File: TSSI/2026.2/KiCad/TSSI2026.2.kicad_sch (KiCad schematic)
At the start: 32 parts, among them J1 Conn_01x02, J2 Conn_01x02, J3 Conn_02x02, Q1 IRLZ34N, T555 Test555, U1 LM555xN, U2 IRLZ34N, U3 4069, U3 IRLZ34N, U4 4001

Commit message: Add files via upload
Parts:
- removed U3: 4069, Package_SO:SOIC-14_3.9x8.7mm_P1.27mm, symbol 4xxx:4069
- removed unit 7 of U3
- added U5: 4069, Package_SO:SOIC-14_3.9x8.7mm_P1.27mm, symbol 4xxx:4069
- U3: footprint Package_SO:SOIC-14_3.9x8.7mm_P1.27mm -> IRLZ34N:TO-220_2_
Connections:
- net GLV: now also U5.14 (VDD)
- net GND: now also U5.7 (VSS)
- net at R3.2: now also U5.1
- net at U4.1: now also U5.2
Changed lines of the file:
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@@
+	)
+	(symbol
+		(lib_id "4xxx:4069")
+		(at 116.84 82.55 0)
+		(unit 7)
+		(exclude_from_sim no)
+		(in_bom yes)
+		(on_board yes)
+		(dnp no)
+		(fields_autoplaced yes)
+		(property "Reference" "U5"
+			(at 123.19 81.2799 0)
+			(effects
+				(font
+					(size 1.27 1.27)
+				)
+				(justify left)
+			)
+		)
+		(property "Value" "4069"
+			(at 123.19 83.8199 0)
+			(effects
+				(font
+					(size 1.27 1.27)
+				)
+				(justify left)
+			)
+		)
+		(property "Footprint" "Package_SO:SOIC-14_3.9x8.7mm_P1.27mm"
+			(at 116.84 82.55 0)
+			(effects
+				(font
+					(size 1.27 1.27)
+				)
+				(hide yes)
+			)
+		)
+		(property "Datasheet" "http://www.intersil.com/content/dam/Intersil/documents/cd40/cd4069ubms.pdf"
+			(at 116.84 82.55 0)
+			(effects
+				(font
+					(size 1.27 1.27)
+				)
+				(hide yes)
+			)
+		)
+		(property "Description" "Hex inverter"
+			(at 116.84 82.55 0)
+			(effects
+				(font
+					(size 1.27 1.27)
+				)
+				(hide yes)
+			)
+		)
+		(pin "7"
+		)
+		(pin "13"
+		)
+		(pin "14"
+		)
+		(pin "12"
+		)
+		(pin "9"
+		)
+		(pin "8"
+		)
+		(pin "10"
+		)
+		(pin "2"
+		)
+		(pin "11"
+		)
+		(pin "3"
+		)
+		(pin "6"
+		)
+		(pin "1"
+		)
+		(pin "4"
+		)
+		(pin "5"
+		)
+		(instances
+			(project ""
+				(path "/d20a762a-d1cd-4658-ba50-73ef390fde04"
+					(reference "U5")
+					(unit 7)
+				)
+			)
+		)
 	)
 	(symbol
@@
 	)
 	(symbol
+		(lib_id "4xxx:4069")
+		(at 88.9 41.91 0)
+		(unit 1)
+		(exclude_from_sim no)
+		(in_bom yes)
+		(on_board yes)
+		(dnp no)
+		(fields_autoplaced yes)
+		(property "Reference" "U5"
+			(at 88.9 33.02 0)
+			(effects
+				(font
+					(size 1.27 1.27)
+				)
+			)
+		)
+		(property "Value" "4069"
+			(at 88.9 35.56 0)
+			(effects
+				(font
+					(size 1.27 1.27)
+				)
+			)
+		)
+		(property "Footprint" "Package_SO:SOIC-14_3.9x8.7mm_P1.27mm"
+			(at 88.9 41.91 0)
+			(effects
+				(font
+					(size 1.27 1.27)
+				)
+				(hide yes)
+			)
+		)
+		(property "Datasheet" "http://www.intersil.com/content/dam/Intersil/documents/cd40/cd4069ubms.pdf"
+			(at 88.9 41.91 0)
+			(effects
+				(font
+					(size 1.27 1.27)
+				)
+				(hide yes)
+			)
+		)
+		(property "Description" "Hex inverter"
+			(at 88.9 41.91 0)
+			(effects
+				(font
+					(size 1.27 1.27)
+				)
+				(hide yes)
+			)
+		)
+		(pin "9"
+		)
+		(pin "3"
+		)
+		(pin "11"
+		)
+		(pin "5"
+		)
+		(pin "12"
+		)
+		(pin "1"
+		)
+		(pin "8"
+		)
+		(pin "2"
+		)
+		(pin "13"
+		)
+		(pin "4"
+		)
+		(pin "7"
+		)
+		(pin "14"
+		)
+		(pin "6"
+		)
+		(pin "10"
+		)
+		(instances
+			(project ""
+				(path "/d20a762a-d1cd-4658-ba50-73ef390fde04"
+					(reference "U5")
+					(unit 1)
+				)
+			)
+		)
+	)
+	(symbol
 		(lib_id "power:GND")
 		(at 67.31 77.47 0)
@@
 	)
 	(symbol
-		(lib_id "4xxx:4069")
-		(at 88.9 41.91 0)
-		(unit 1)
-		(exclude_from_sim no)
-		(in_bom yes)
-		(on_board yes)
-		(dnp no)
-		(fields_autoplaced yes)
-		(property "Reference" "U3"
-			(at 88.9 33.02 0)
-			(effects
-				(font
-					(size 1.27 1.27)
-				)
-			)
-		)
-		(property "Value" "4069"
-			(at 88.9 35.56 0)
-			(effects
-				(font
-					(size 1.27 1.27)
-				)
-			)
-		)
-		(property "Footprint" "Package_SO:SOIC-14_3.9x8.7mm_P1.27mm"
-			(at 88.9 41.91 0)
-			(effects
-				(font
-					(size 1.27 1.27)
-				)
-				(hide yes)
-			)
-		)
-		(property "Datasheet" "http://www.intersil.com/content/dam/Intersil/documents/cd40/cd4069ubms.pdf"
-			(at 88.9 41.91 0)
-			(effects
-				(font
-					(size 1.27 1.27)
-				)
-				(hide yes)
-			)
-		)
-		(property "Description" "Hex inverter"
-			(at 88.9 41.91 0)
-			(effects
-				(font
-					(size 1.27 1.27)
-				)
-				(hide yes)
-			)
-		)
-		(pin "3"
-		)
-		(pin "14"
-		)
-		(pin "4"
-		)
-		(pin "11"
-		)
-		(pin "13"
-		)
-		(pin "6"
-		)
-		(pin "5"
-		)
-		(pin "9"
-		)
-		(pin "8"
-		)
-		(pin "10"
-		)
-		(pin "1"
-		)
-		(pin "2"
-		)
-		(pin "12"
-		)
-		(pin "7"
-		)
-		(instances
-			(project ""
-				(path "/d20a762a-d1cd-4658-ba50-73ef390fde04"
-					(reference "U3")
-					(unit 1)
-				)
-			)
-		)
-	)
-	(symbol
 		(lib_id "Timer:LM555xN")
 		(at 209.55 68.58 0)
@@
 			)
 		)
-		(property "Footprint" "Package_SO:SOIC-14_3.9x8.7mm_P1.27mm"
+		(property "Footprint" "IRLZ34N:TO-220_2_"
 			(at 237.49 63.5 0)
 			(effects
@@
 				)
 			)
-		)
-	)
-	(symbol
-		(lib_id "4xxx:4069")
-		(at 116.84 82.55 0)
-		(unit 7)
-		(exclude_from_sim no)
-		(in_bom yes)
-		(on_board yes)
-		(dnp no)
-		(fields_autoplaced yes)
-		(property "Reference" "U3"
-			(at 123.19 81.2799 0)
-			(effects
-				(font
-					(size 1.27 1.27)
-				)
-				(justify left)
-			)
-		)
-		(property "Value" "4069"
-			(at 123.19 83.8199 0)
-			(effects
-				(font
-					(size 1.27 1.27)
-				)
-				(justify left)
-			)
-		)
-		(property "Footprint" "Package_SO:SOIC-14_3.9x8.7mm_P1.27mm"
-			(at 116.84 82.55 0)
-			(effects
-				(font
-					(size 1.27 1.27)
-				)
-				(hide yes)
-			)
-		)
-		(property "Datasheet" "http://www.intersil.com/content/dam/Intersil/documents/cd40/cd4069ubms.pdf"
-			(at 116.84 82.55 0)
-			(effects
-				(font
-					(size 1.27 1.27)
-				)
-				(hide yes)
-			)
-		)
-		(property "Description" "Hex inverter"
-			(at 116.84 82.55 0)
-			(effects
-				(font
-					(size 1.27 1.27)
-				)
-				(hide yes)
-			)
-		)
-		(pin "5"
-		)
-		(pin "2"
-		)
-		(pin "12"
-		)
-		(pin "11"
-		)
-		(pin "3"
-		)
-		(pin "7"
-		)
-		(pin "1"
-		)
-		(pin "6"
-		)
-		(pin "10"
-		)
-		(pin "4"
-		)
-		(pin "14"
-		)
-		(pin "9"
-		)
-		(pin "13"
-		)
-		(pin "8"
-		)
-		(instances
-			(project ""
-				(path "/d20a762a-d1cd-4658-ba50-73ef390fde04"
-					(reference "U3")
-					(unit 7)
-				)
-			)

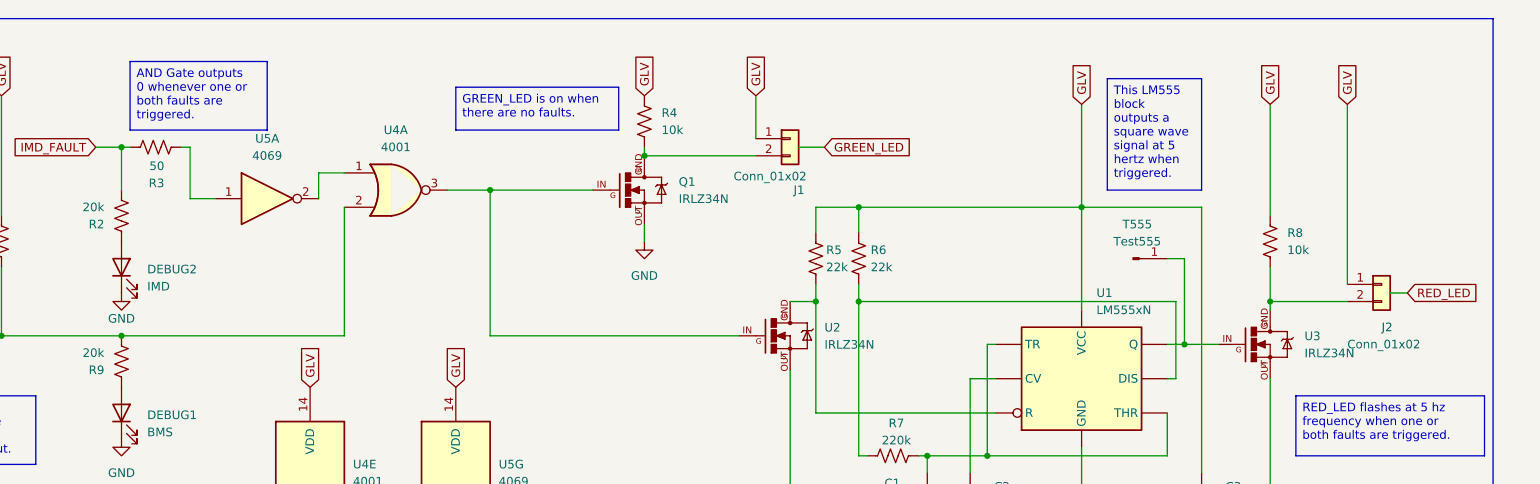
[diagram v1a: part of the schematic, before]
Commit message: Update TSSI_2026.2
Removed 12V for lights and condensed to 2 pin for one light and the other
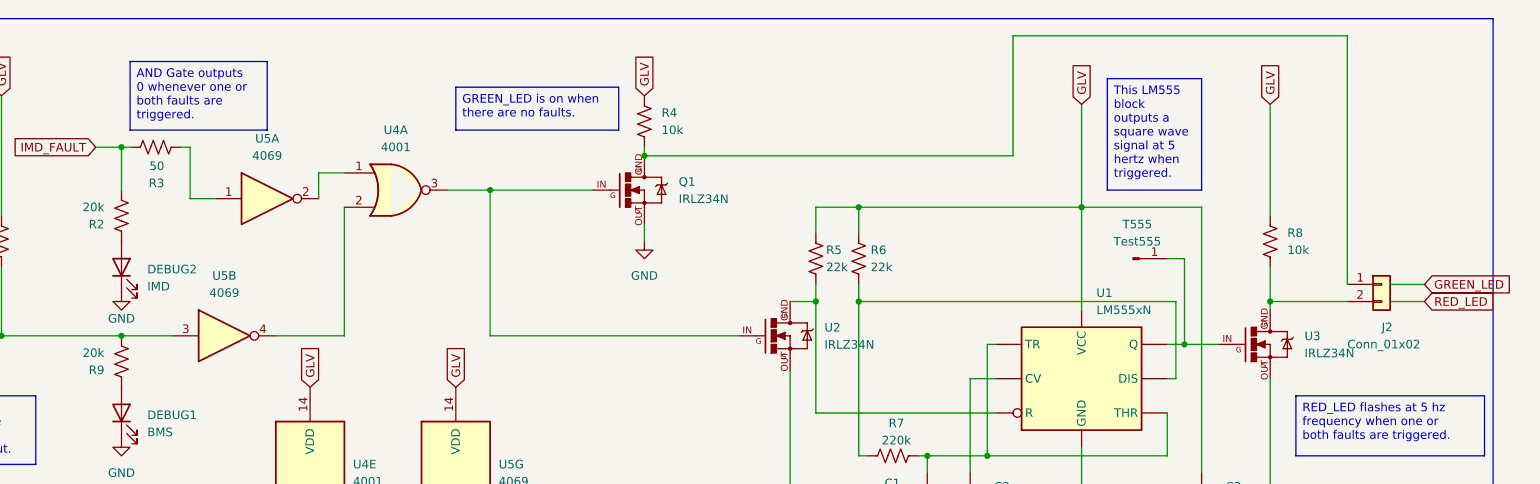
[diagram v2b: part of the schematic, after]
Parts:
- removed J1: Conn_01x02, Connector_Molex:Molex_Mini-Fit_Jr_5566-02A_2x01_P4.20mm_Vertical, symbol Connector_Generic:Conn_01x02
- added unit 2 of U5
- Q1, U2, U3: footprint IRLZ34N:TO-220_2_ -> Anteater-Electric-Racing electrical-pcbs main TSSI-2026.2_KiCad_Parts_IRLZ34N:TO-220_2_
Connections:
- net BMS_FAULT: now also U5.3; no longer U4.2
- net GLV: no longer J2.1 (Pin_1)
- net at Q1.GND, R4.2: now also J2.1 (Pin_1)
- new net: U4.2, U5.4

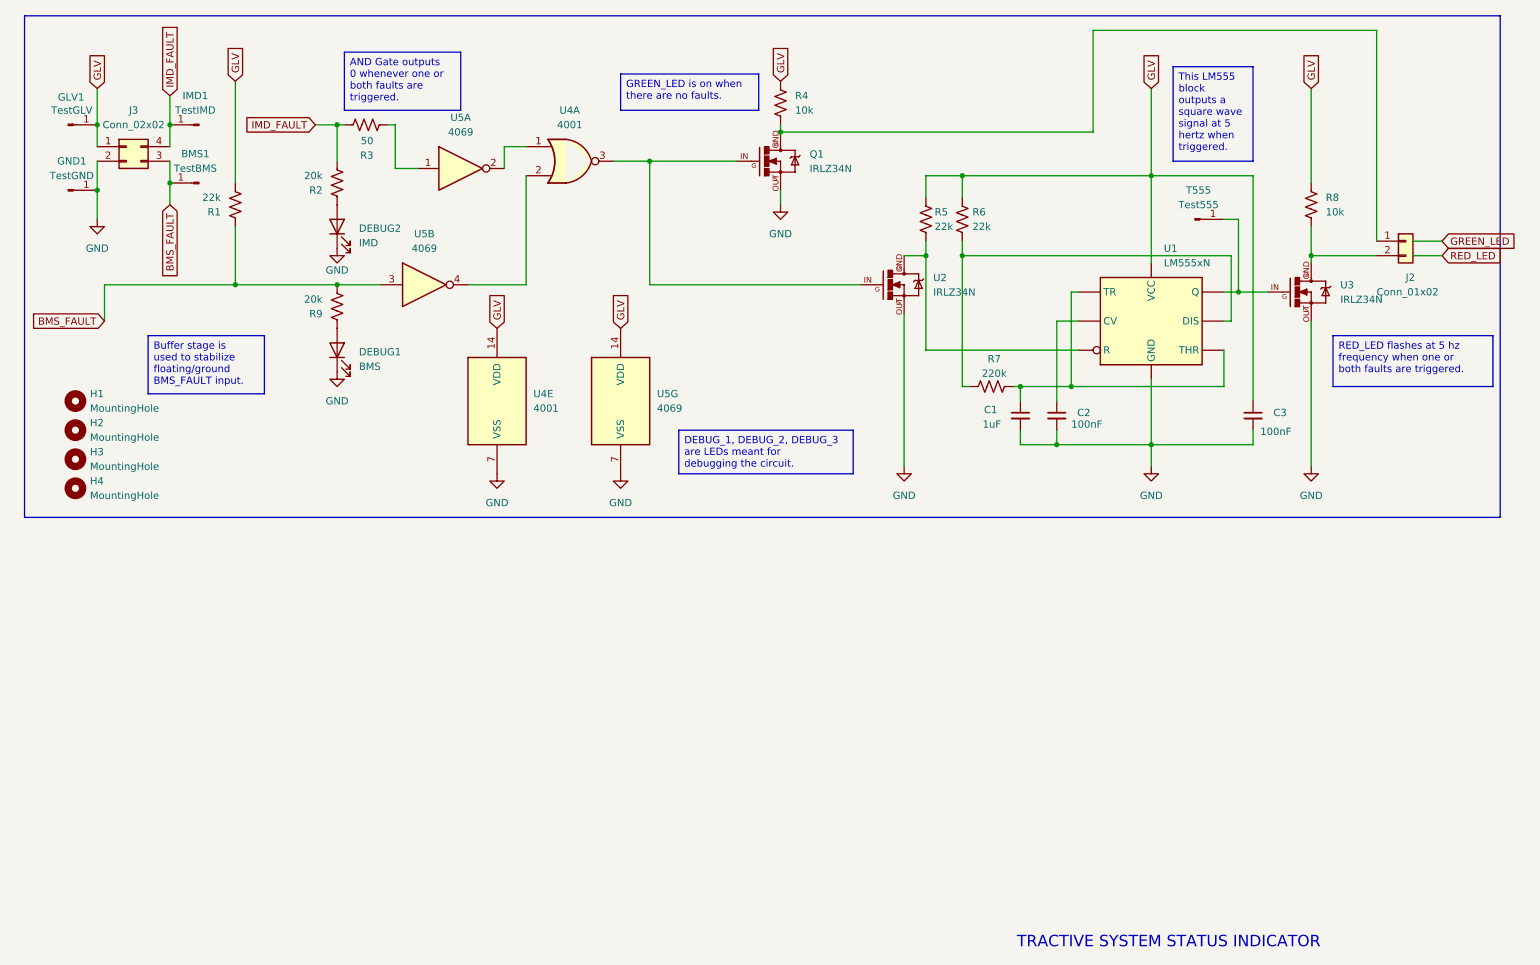
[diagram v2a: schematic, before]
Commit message: connected remaining pins to gnd
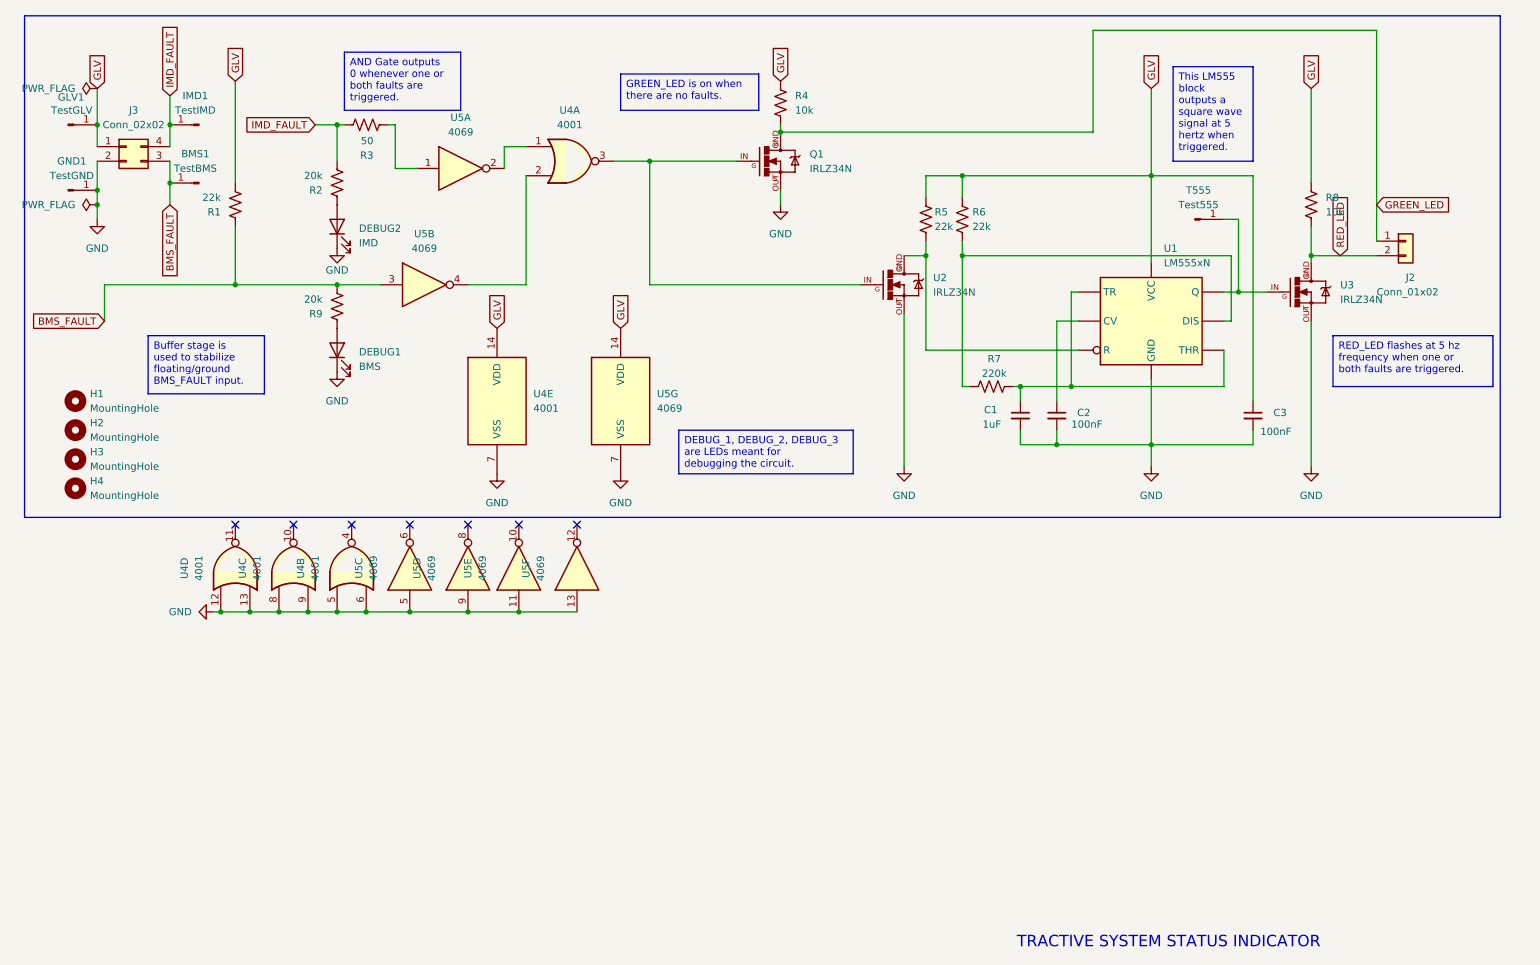
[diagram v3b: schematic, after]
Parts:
- added unit 2 of U4
- added unit 4 of U4
- added unit 3 of U4
- added unit 5 of U5
- added unit 3 of U5
- added unit 6 of U5
- added unit 4 of U5
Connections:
- net GND: now also U4.12, U4.13, U4.5, U4.6, U4.8, U4.9, U5.11, U5.13, U5.5, U5.9
- net GREEN_LED: now also J2.1 (Pin_1), Q1.GND, R4.2
- net RED_LED: now also J2.2 (Pin_2), R8.2, U3.GND
- no-connect marks 0 -> 7
